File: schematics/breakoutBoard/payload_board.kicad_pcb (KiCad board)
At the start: 2 copper layers, 75 x 107 mm, 19 parts, among them P1 CONN_02X50, P2 CONN_02X50, P3 CONN_02X50, P4 CONN_02X50, U1 breakout_carrier

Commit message: 'final' push
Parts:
- removed RIB1: B5B-EH-A, breakoutBoard:B5B-EH-A
- added SMA2: Molex-MMCX-SMD, breakoutBoard:Molex MMCX SMD 50Ohm, F.Cu at (113.0, 154.0)
- added e1: ribbon2.54mmPitch, breakoutBoard:ribbon2.5mmPitch, F.Cu at (87.4, 154.2)
- moved SMA1 6.17 mm to (103.0, 154.0)
- moved U1 4.46 mm to (61.0, 153.2)
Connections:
- P1 pad 79: Net-(P1-Pad79) -> Net-(P1-Pad78)
- P1 pad 80: Net-(P1-Pad80) -> Net-(P1-Pad78)
- P1 pad 95: Net-(P1-Pad95) -> Net-(P1-Pad78)
- P2 pad 78: Net-(P2-Pad78) -> Net-(P1-Pad78)
- P2 pad 79: Net-(P2-Pad79) -> Net-(P1-Pad78)
- P2 pad 80: Net-(P2-Pad80) -> Net-(P1-Pad78)
- P2 pad 98: Net-(P2-Pad98) -> Net-(P1-Pad78)
- P3 pad 11: Net-(P3-Pad11) -> Net-(P1-Pad78)
- P3 pad 30: Net-(P3-Pad30) -> Net-(P1-Pad78)
- P3 pad 32: Net-(P3-Pad32) -> Net-(P1-Pad78)
- P3 pad 45: Net-(P3-Pad45) -> Net-(P1-Pad78)
- P3 pad 46: Net-(P3-Pad46) -> Net-(P1-Pad78)
- P3 pad 5: Net-(P3-Pad5) -> Net-(P1-Pad78)
- P3 pad 7: Net-(P3-Pad7) -> Net-(P1-Pad78)
- P3 pad 9: Net-(P3-Pad9) -> Net-(P1-Pad78)
- SMA1 pad 1: Net-(P1-Pad92) -> Net-(SMA1-Pad1)
- SMA1 pad 2: Net-(P1-Pad94) -> Net-(SMA1-Pad2)
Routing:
- net Net-(P1-Pad78): track 0.00 -> 257.8 mm, vias 0 -> 1
- net Net-(P4-Pad99): track 0.00 -> 68.2 mm
- net Net-(P1-Pad95): track 63.9 -> 0.00 mm, vias 1 -> 0
- net Net-(P4-Pad98): track 0.00 -> 51.8 mm
- net Net-(P2-Pad17): track 100.6 -> 115.0 mm
- net Net-(SMA1-Pad1): track 0.00 -> 10.0 mm
- net Net-(P1-Pad5): track 110.9 -> 115.7 mm
- net Net-(P1-Pad57): track 146.3 -> 143.3 mm, vias 2 -> 3
- net Net-(P2-Pad19): track 103.3 -> 100.8 mm, vias 0 -> 1
- added copper zone on B.Cu, net Net-(SMA1-Pad2)
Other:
- board text added: "5V"
- board text added: "CySat 488 Team: Trent Allison Brian Bradford"
- board text added: "Jared Danner Leo Freier"
- board text added: "UARTRX"
- board text added: "UARTTX"

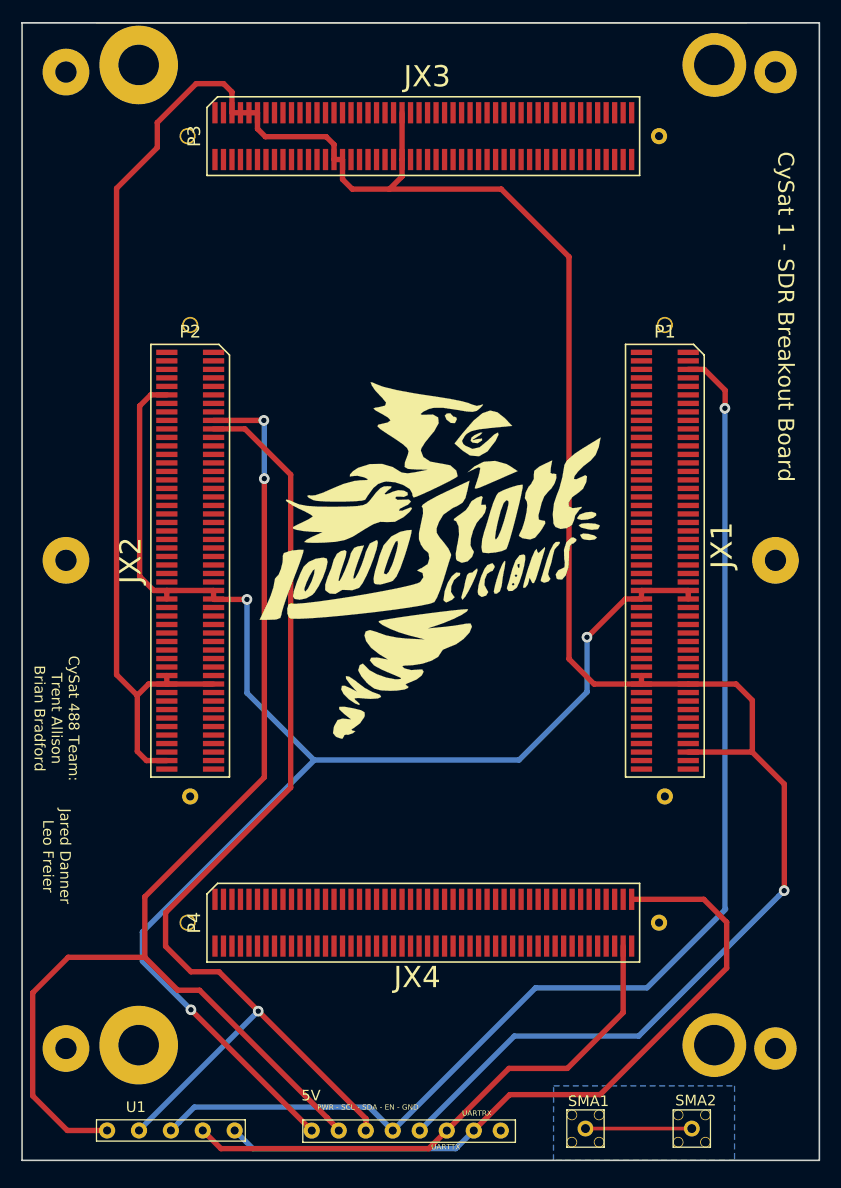
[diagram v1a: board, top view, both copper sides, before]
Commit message: final board v2, now with UART
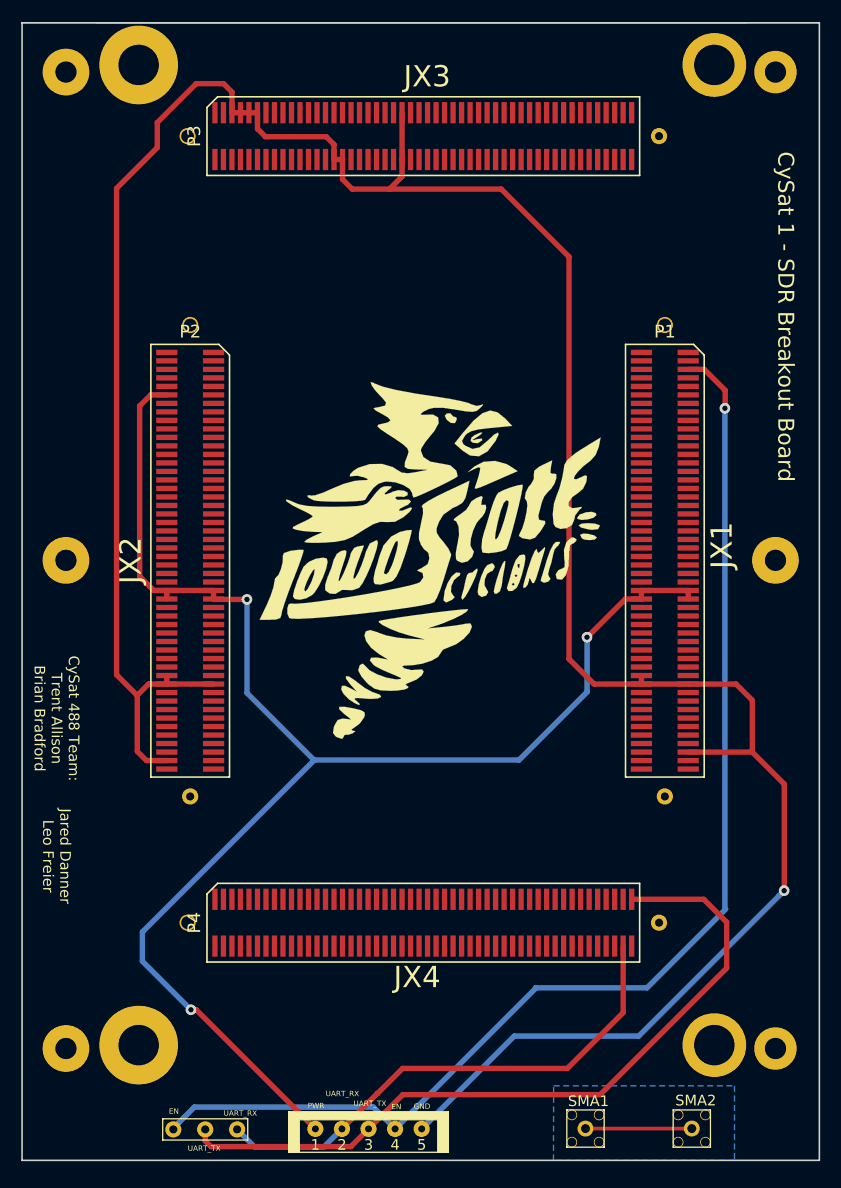
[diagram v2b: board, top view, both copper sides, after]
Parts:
- removed e1: ribbon2.54mmPitch, breakoutBoard:ribbon2.5mmPitch
- added RIB1: B5B-EH-A, breakoutBoard:B5B-EH-A, F.Cu at (75.1, 152.4)
- moved U1 6.23 mm to (67.2, 153.1)
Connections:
- U1 pad 1: Net-(P2-Pad17) -> Net-(P1-Pad5)
- U1 pad 2: Net-(P2-Pad19) -> Net-(P4-Pad99)
- U1 pad 3: Net-(P1-Pad5) -> Net-(P4-Pad98)
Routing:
- net Net-(P2-Pad17): track 115.0 -> 0.00 mm, vias 2 -> 0
- net Net-(P2-Pad19): track 100.8 -> 0.00 mm, vias 1 -> 0
- net Net-(P4-Pad98): track 51.8 -> 48.5 mm
- net Net-(P4-Pad99): track 68.2 -> 71.5 mm
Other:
- board text added: "EN"
- board text added: "GND"
- board text added: "PWR"
- board text added: "UART_RX"
- board text added: "UART_TX"
- board text removed: "5V"
- board text removed: "PWR - SCL - SDA - EN - GND"
- board text removed: "UARTRX"
- board text removed: "UARTTX"

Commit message: Files updated based on recent version sent to fab house
This more recent revision fixes the FPGA connector issue and adds the LNA board to the backside. Board was changed from a 2-layer to a 4-layer board due to the additional RF components added.
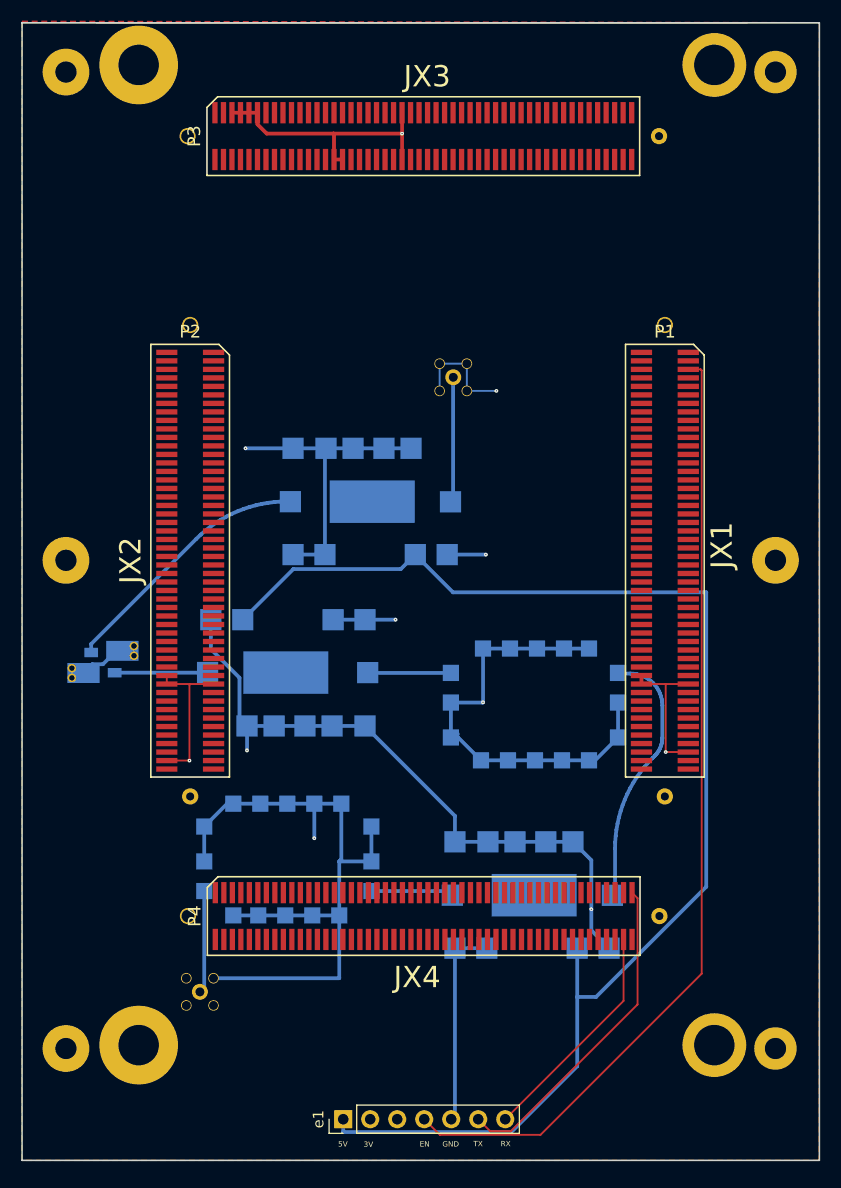
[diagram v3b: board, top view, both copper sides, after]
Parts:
- removed G*** (x2): LOGO, breakoutBoard:Cysized
- removed RIB1: B5B-EH-A, breakoutBoard:B5B-EH-A
- added U2: TAMP, mini-circuits:MCL, B.Cu at (98.0, 132.1)
- added U3: CBP, mini-circuits:CBP, B.Cu at (98.4, 113.9)
- added U4: TAMP, mini-circuits:MCL, B.Cu at (74.9, 111.1)
- added U5: LAT-3, RF_Mini-Circuits:Mini-Circuits_MMM168_LandPatternPL-225, B.Cu at (57.6, 110.2)
- added U6: TAMP, mini-circuits:MCL, B.Cu at (82.8, 95.1)
- added e1: ribbon2.54mmPitch, Connector_PinHeader_2.54mm:PinHeader_1x07_P2.54mm_Vertical, F.Cu at (80.2, 153.1)
- SMA1, SMA2: moved to B.Cu
- U1: value breakout_carrier -> CBP; footprint breakoutBoard:breakout_carrier -> mini-circuits:CBP; moved to B.Cu
- moved SMA2 74.1 mm to (90.6, 83.3)
- moved SMA1 38.5 mm to (66.7, 141.2)
- moved U1 25.4 mm to (74.8, 128.9)
- moved P4 0.63 mm to (87.8, 134.0)
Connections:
- net Net-(P1-Pad57) renamed 3V
- net Net-(P1-Pad78) renamed GND
- P1 pad 1: Net-(P1-Pad1) -> (no net)
- P1 pad 10: Net-(P1-Pad10) -> (no net)
- P1 pad 100: Net-(P1-Pad100) -> (no net)
- P1 pad 11: Net-(P1-Pad11) -> (no net)
- P1 pad 12: Net-(P1-Pad12) -> (no net)
- P1 pad 13: Net-(P1-Pad13) -> (no net)
- P1 pad 14: Net-(P1-Pad14) -> (no net)
- P1 pad 15: Net-(P1-Pad15) -> (no net)
- P1 pad 16: Net-(P1-Pad16) -> (no net)
- P1 pad 17: Net-(P1-Pad17) -> (no net)
- P1 pad 18: Net-(P1-Pad18) -> (no net)
- P1 pad 19: Net-(P1-Pad19) -> (no net)
- P1 pad 2: Net-(P1-Pad2) -> (no net)
- P1 pad 20: Net-(P1-Pad20) -> (no net)
- P1 pad 21: Net-(P1-Pad21) -> (no net)
- P1 pad 22: Net-(P1-Pad22) -> (no net)
- P1 pad 23: Net-(P1-Pad23) -> (no net)
- P1 pad 24: Net-(P1-Pad24) -> (no net)
- P1 pad 25: Net-(P1-Pad25) -> (no net)
- P1 pad 26: Net-(P1-Pad26) -> (no net)
- P1 pad 27: Net-(P1-Pad27) -> (no net)
- P1 pad 28: Net-(P1-Pad28) -> (no net)
- P1 pad 29: Net-(P1-Pad29) -> (no net)
- P1 pad 3: Net-(P1-Pad3) -> (no net)
- P1 pad 30: Net-(P1-Pad30) -> (no net)
- P1 pad 31: Net-(P1-Pad31) -> (no net)
- P1 pad 32: Net-(P1-Pad32) -> (no net)
- P1 pad 33: Net-(P1-Pad33) -> (no net)
- P1 pad 34: Net-(P1-Pad34) -> (no net)
- P1 pad 35: Net-(P1-Pad35) -> (no net)
- P1 pad 36: Net-(P1-Pad36) -> (no net)
- P1 pad 37: Net-(P1-Pad37) -> (no net)
- P1 pad 38: Net-(P1-Pad38) -> (no net)
- P1 pad 39: Net-(P1-Pad39) -> (no net)
- P1 pad 4: Net-(P1-Pad4) -> (no net)
- P1 pad 40: Net-(P1-Pad40) -> (no net)
- P1 pad 41: Net-(P1-Pad41) -> (no net)
- P1 pad 42: Net-(P1-Pad42) -> (no net)
- P1 pad 43: Net-(P1-Pad43) -> (no net)
- P1 pad 44: Net-(P1-Pad44) -> (no net)
- P1 pad 45: Net-(P1-Pad45) -> (no net)
- P1 pad 46: Net-(P1-Pad46) -> (no net)
- P1 pad 47: Net-(P1-Pad47) -> (no net)
- P1 pad 48: Net-(P1-Pad48) -> (no net)
- P1 pad 49: Net-(P1-Pad49) -> (no net)
- P1 pad 5: Net-(P1-Pad5) -> EN
- P1 pad 50: Net-(P1-Pad50) -> (no net)
- P1 pad 51: Net-(P1-Pad51) -> (no net)
- P1 pad 52: Net-(P1-Pad52) -> (no net)
- P1 pad 53: Net-(P1-Pad53) -> (no net)
- P1 pad 54: Net-(P1-Pad54) -> (no net)
- P1 pad 55: Net-(P1-Pad55) -> (no net)
- P1 pad 56: Net-(P1-Pad56) -> (no net)
- P1 pad 6: Net-(P1-Pad6) -> (no net)
- P1 pad 61: Net-(P1-Pad61) -> (no net)
- P1 pad 62: Net-(P1-Pad62) -> (no net)
- P1 pad 63: Net-(P1-Pad63) -> (no net)
- P1 pad 64: Net-(P1-Pad64) -> (no net)
- P1 pad 65: Net-(P1-Pad65) -> (no net)
- P1 pad 66: Net-(P1-Pad66) -> (no net)
- P1 pad 67: Net-(P1-Pad67) -> (no net)
- P1 pad 68: Net-(P1-Pad68) -> (no net)
- P1 pad 69: Net-(P1-Pad69) -> (no net)
- P1 pad 7: Net-(P1-Pad7) -> (no net)
- P1 pad 70: Net-(P1-Pad70) -> (no net)
- P1 pad 71: Net-(P1-Pad71) -> (no net)
- P1 pad 72: Net-(P1-Pad72) -> (no net)
- P1 pad 73: Net-(P1-Pad73) -> (no net)
- P1 pad 74: Net-(P1-Pad74) -> (no net)
- P1 pad 75: Net-(P1-Pad75) -> (no net)
- P1 pad 76: Net-(P1-Pad76) -> (no net)
- P1 pad 77: Net-(P1-Pad77) -> (no net)
- P1 pad 8: Net-(P1-Pad8) -> (no net)
- P1 pad 81: Net-(P1-Pad81) -> (no net)
- P1 pad 82: Net-(P1-Pad82) -> (no net)
- P1 pad 83: Net-(P1-Pad83) -> (no net)
- P1 pad 84: Net-(P1-Pad84) -> (no net)
- P1 pad 85: Net-(P1-Pad85) -> (no net)
- P1 pad 86: Net-(P1-Pad86) -> (no net)
- P1 pad 87: Net-(P1-Pad87) -> (no net)
- P1 pad 88: Net-(P1-Pad88) -> (no net)
- P1 pad 89: Net-(P1-Pad89) -> (no net)
- P1 pad 9: Net-(P1-Pad9) -> (no net)
- P1 pad 90: Net-(P1-Pad90) -> (no net)
- P1 pad 91: Net-(P1-Pad91) -> (no net)
- P1 pad 92: Net-(P1-Pad92) -> (no net)
- P1 pad 93: Net-(P1-Pad93) -> (no net)
- P1 pad 94: Net-(P1-Pad94) -> (no net)
- P1 pad 96: Net-(P1-Pad96) -> (no net)
- P1 pad 97: Net-(P1-Pad97) -> (no net)
- P1 pad 98: Net-(P1-Pad98) -> (no net)
- P1 pad 99: Net-(P1-Pad99) -> (no net)
- P2 pad 1: Net-(P2-Pad1) -> (no net)
- P2 pad 10: Net-(P2-Pad10) -> (no net)
- P2 pad 100: Net-(P2-Pad100) -> (no net)
- P2 pad 11: Net-(P2-Pad11) -> (no net)
- P2 pad 13: Net-(P2-Pad13) -> (no net)
- P2 pad 14: Net-(P2-Pad14) -> (no net)
- P2 pad 15: Net-(P2-Pad15) -> (no net)
- P2 pad 16: Net-(P2-Pad16) -> (no net)
- P2 pad 17: Net-(P2-Pad17) -> (no net)
- P2 pad 18: Net-(P2-Pad18) -> (no net)
- P2 pad 19: Net-(P2-Pad19) -> (no net)
- P2 pad 2: Net-(P2-Pad2) -> (no net)
- P2 pad 20: Net-(P2-Pad20) -> (no net)
- P2 pad 21: Net-(P2-Pad21) -> (no net)
- P2 pad 22: Net-(P2-Pad22) -> (no net)
- P2 pad 23: Net-(P2-Pad23) -> (no net)
- P2 pad 24: Net-(P2-Pad24) -> (no net)
- P2 pad 25: Net-(P2-Pad25) -> (no net)
- P2 pad 26: Net-(P2-Pad26) -> (no net)
- P2 pad 27: Net-(P2-Pad27) -> (no net)
- P2 pad 28: Net-(P2-Pad28) -> (no net)
- P2 pad 29: Net-(P2-Pad29) -> (no net)
- P2 pad 3: Net-(P2-Pad3) -> (no net)
- P2 pad 30: Net-(P2-Pad30) -> (no net)
- P2 pad 31: Net-(P2-Pad31) -> (no net)
- P2 pad 32: Net-(P2-Pad32) -> (no net)
- P2 pad 33: Net-(P2-Pad33) -> (no net)
- P2 pad 34: Net-(P2-Pad34) -> (no net)
- P2 pad 35: Net-(P2-Pad35) -> (no net)
- P2 pad 36: Net-(P2-Pad36) -> (no net)
- P2 pad 37: Net-(P2-Pad37) -> (no net)
- P2 pad 38: Net-(P2-Pad38) -> (no net)
- P2 pad 39: Net-(P2-Pad39) -> (no net)
- P2 pad 4: Net-(P2-Pad4) -> (no net)
- P2 pad 40: Net-(P2-Pad40) -> (no net)
- P2 pad 41: Net-(P2-Pad41) -> (no net)
- P2 pad 42: Net-(P2-Pad42) -> (no net)
- P2 pad 43: Net-(P2-Pad43) -> (no net)
- P2 pad 44: Net-(P2-Pad44) -> (no net)
- P2 pad 45: Net-(P2-Pad45) -> (no net)
- P2 pad 46: Net-(P2-Pad46) -> (no net)
- P2 pad 47: Net-(P2-Pad47) -> (no net)
- P2 pad 48: Net-(P2-Pad48) -> (no net)
- P2 pad 49: Net-(P2-Pad49) -> (no net)
- P2 pad 5: Net-(P2-Pad5) -> (no net)
- P2 pad 50: Net-(P2-Pad50) -> (no net)
- P2 pad 51: Net-(P2-Pad51) -> (no net)
- P2 pad 52: Net-(P2-Pad52) -> (no net)
- P2 pad 53: Net-(P2-Pad53) -> (no net)
- P2 pad 54: Net-(P2-Pad54) -> (no net)
- P2 pad 55: Net-(P2-Pad55) -> (no net)
- P2 pad 56: Net-(P2-Pad56) -> (no net)
- P2 pad 6: Net-(P2-Pad6) -> (no net)
- P2 pad 61: Net-(P2-Pad61) -> (no net)
- P2 pad 62: Net-(P2-Pad62) -> (no net)
- P2 pad 63: Net-(P2-Pad63) -> (no net)
- P2 pad 64: Net-(P2-Pad64) -> (no net)
- P2 pad 65: Net-(P2-Pad65) -> (no net)
- P2 pad 66: Net-(P2-Pad66) -> (no net)
- P2 pad 67: Net-(P2-Pad67) -> (no net)
- P2 pad 68: Net-(P2-Pad68) -> (no net)
- P2 pad 69: Net-(P2-Pad69) -> (no net)
- P2 pad 7: Net-(P2-Pad7) -> (no net)
- P2 pad 70: Net-(P2-Pad70) -> (no net)
- P2 pad 71: Net-(P2-Pad71) -> (no net)
- P2 pad 72: Net-(P2-Pad72) -> (no net)
- P2 pad 73: Net-(P2-Pad73) -> (no net)
- P2 pad 74: Net-(P2-Pad74) -> (no net)
- P2 pad 75: Net-(P2-Pad75) -> (no net)
- P2 pad 76: Net-(P2-Pad76) -> (no net)
- P2 pad 77: Net-(P2-Pad77) -> (no net)
- P2 pad 8: Net-(P2-Pad8) -> (no net)
- P2 pad 81: Net-(P2-Pad81) -> (no net)
- P2 pad 82: Net-(P2-Pad82) -> (no net)
- P2 pad 83: Net-(P2-Pad83) -> (no net)
- P2 pad 84: Net-(P2-Pad84) -> (no net)
- P2 pad 85: Net-(P2-Pad85) -> (no net)
- P2 pad 86: Net-(P2-Pad86) -> (no net)
- P2 pad 87: Net-(P2-Pad87) -> (no net)
- P2 pad 88: Net-(P2-Pad88) -> (no net)
- P2 pad 89: Net-(P2-Pad89) -> (no net)
- P2 pad 9: Net-(P2-Pad9) -> (no net)
- P2 pad 90: Net-(P2-Pad90) -> (no net)
- P2 pad 91: Net-(P2-Pad91) -> (no net)
- P2 pad 92: Net-(P2-Pad92) -> (no net)
- P2 pad 93: Net-(P2-Pad93) -> (no net)
- P2 pad 94: Net-(P2-Pad94) -> (no net)
- P2 pad 95: Net-(P2-Pad95) -> (no net)
- P2 pad 96: Net-(P2-Pad96) -> (no net)
- P2 pad 97: Net-(P2-Pad97) -> (no net)
- P2 pad 99: Net-(P2-Pad99) -> (no net)
- P3 pad 1: Net-(P3-Pad1) -> (no net)
- P3 pad 10: Net-(P3-Pad10) -> (no net)
- P3 pad 100: Net-(P3-Pad100) -> (no net)
- P3 pad 12: Net-(P3-Pad12) -> (no net)
- P3 pad 13: Net-(P3-Pad13) -> (no net)
- P3 pad 14: Net-(P3-Pad14) -> (no net)
- P3 pad 15: Net-(P3-Pad15) -> (no net)
- P3 pad 16: Net-(P3-Pad16) -> (no net)
- P3 pad 17: Net-(P3-Pad17) -> (no net)
- P3 pad 18: Net-(P3-Pad18) -> (no net)
- P3 pad 19: Net-(P3-Pad19) -> (no net)
- P3 pad 2: Net-(P3-Pad2) -> (no net)
- P3 pad 20: Net-(P3-Pad20) -> (no net)
- P3 pad 21: Net-(P3-Pad21) -> (no net)
- P3 pad 22: Net-(P3-Pad22) -> (no net)
- P3 pad 23: Net-(P3-Pad23) -> (no net)
- P3 pad 24: Net-(P3-Pad24) -> (no net)
- P3 pad 25: Net-(P3-Pad25) -> (no net)
- P3 pad 26: Net-(P3-Pad26) -> (no net)
- P3 pad 27: Net-(P3-Pad27) -> (no net)
- P3 pad 28: Net-(P3-Pad28) -> (no net)
- P3 pad 29: Net-(P3-Pad29) -> (no net)
- P3 pad 3: Net-(P3-Pad3) -> (no net)
- P3 pad 31: Net-(P3-Pad31) -> (no net)
- P3 pad 33: Net-(P3-Pad33) -> (no net)
- P3 pad 34: Net-(P3-Pad34) -> (no net)
- P3 pad 35: Net-(P3-Pad35) -> (no net)
- P3 pad 36: Net-(P3-Pad36) -> (no net)
- P3 pad 37: Net-(P3-Pad37) -> (no net)
- P3 pad 38: Net-(P3-Pad38) -> (no net)
- P3 pad 39: Net-(P3-Pad39) -> (no net)
- P3 pad 4: Net-(P3-Pad4) -> (no net)
- P3 pad 40: Net-(P3-Pad40) -> (no net)
- P3 pad 41: Net-(P3-Pad41) -> (no net)
- P3 pad 42: Net-(P3-Pad42) -> (no net)
- P3 pad 43: Net-(P3-Pad43) -> (no net)
- P3 pad 44: Net-(P3-Pad44) -> (no net)
- P3 pad 47: Net-(P3-Pad47) -> (no net)
- P3 pad 48: Net-(P3-Pad48) -> (no net)
- P3 pad 49: Net-(P3-Pad49) -> (no net)
- P3 pad 50: Net-(P3-Pad50) -> (no net)
- P3 pad 51: Net-(P3-Pad51) -> (no net)
- P3 pad 52: Net-(P3-Pad52) -> (no net)
- P3 pad 53: Net-(P3-Pad53) -> (no net)
- P3 pad 54: Net-(P3-Pad54) -> (no net)
- P3 pad 55: Net-(P3-Pad55) -> (no net)
- P3 pad 56: Net-(P3-Pad56) -> (no net)
- P3 pad 57: Net-(P3-Pad57) -> (no net)
- P3 pad 58: Net-(P3-Pad58) -> (no net)
- P3 pad 59: Net-(P3-Pad59) -> (no net)
- P3 pad 6: Net-(P3-Pad6) -> (no net)
- P3 pad 60: Net-(P3-Pad60) -> (no net)
- P3 pad 61: Net-(P3-Pad61) -> (no net)
- P3 pad 62: Net-(P3-Pad62) -> (no net)
- P3 pad 63: Net-(P3-Pad63) -> (no net)
- P3 pad 64: Net-(P3-Pad64) -> (no net)
- P3 pad 65: Net-(P3-Pad65) -> (no net)
- P3 pad 66: Net-(P3-Pad66) -> (no net)
- P3 pad 67: Net-(P3-Pad67) -> (no net)
- P3 pad 68: Net-(P3-Pad68) -> (no net)
- P3 pad 69: Net-(P3-Pad69) -> (no net)
- P3 pad 70: Net-(P3-Pad70) -> (no net)
- P3 pad 71: Net-(P3-Pad71) -> (no net)
- P3 pad 72: Net-(P3-Pad72) -> (no net)
- P3 pad 73: Net-(P3-Pad73) -> (no net)
- P3 pad 74: Net-(P3-Pad74) -> (no net)
- P3 pad 75: Net-(P3-Pad75) -> (no net)
- P3 pad 76: Net-(P3-Pad76) -> (no net)
- P3 pad 77: Net-(P3-Pad77) -> (no net)
- P3 pad 78: Net-(P3-Pad78) -> (no net)
- P3 pad 79: Net-(P3-Pad79) -> (no net)
- P3 pad 8: Net-(P3-Pad8) -> (no net)
- P3 pad 80: Net-(P3-Pad80) -> (no net)
- P3 pad 81: Net-(P3-Pad81) -> (no net)
- P3 pad 82: Net-(P3-Pad82) -> (no net)
- P3 pad 83: Net-(P3-Pad83) -> (no net)
- P3 pad 84: Net-(P3-Pad84) -> (no net)
- P3 pad 85: Net-(P3-Pad85) -> (no net)
- P3 pad 86: Net-(P3-Pad86) -> (no net)
- P3 pad 87: Net-(P3-Pad87) -> (no net)
- P3 pad 88: Net-(P3-Pad88) -> (no net)
- P3 pad 89: Net-(P3-Pad89) -> (no net)
- P3 pad 90: Net-(P3-Pad90) -> (no net)
- P3 pad 91: Net-(P3-Pad91) -> (no net)
- P3 pad 92: Net-(P3-Pad92) -> (no net)
- P3 pad 93: Net-(P3-Pad93) -> (no net)
- P3 pad 94: Net-(P3-Pad94) -> (no net)
- P3 pad 95: Net-(P3-Pad95) -> (no net)
- P3 pad 96: Net-(P3-Pad96) -> (no net)
- P3 pad 97: Net-(P3-Pad97) -> (no net)
- P3 pad 98: Net-(P3-Pad98) -> (no net)
- P3 pad 99: Net-(P3-Pad99) -> (no net)
- P4 pad 1: Net-(P4-Pad1) -> (no net)
- P4 pad 10: Net-(P4-Pad10) -> (no net)
- P4 pad 100: Net-(P4-Pad100) -> (no net)
- P4 pad 11: Net-(P4-Pad11) -> (no net)
- P4 pad 12: Net-(P4-Pad12) -> (no net)
- P4 pad 13: Net-(P4-Pad13) -> (no net)
- P4 pad 14: Net-(P4-Pad14) -> (no net)
- P4 pad 15: Net-(P4-Pad15) -> (no net)
- P4 pad 16: Net-(P4-Pad16) -> (no net)
- P4 pad 17: Net-(P4-Pad17) -> (no net)
- P4 pad 18: Net-(P4-Pad18) -> (no net)
- P4 pad 19: Net-(P4-Pad19) -> (no net)
- P4 pad 2: Net-(P4-Pad2) -> (no net)
- P4 pad 20: Net-(P4-Pad20) -> (no net)
- P4 pad 21: Net-(P4-Pad21) -> (no net)
- P4 pad 22: Net-(P4-Pad22) -> (no net)
- P4 pad 23: Net-(P4-Pad23) -> (no net)
- P4 pad 24: Net-(P4-Pad24) -> (no net)
- P4 pad 25: Net-(P4-Pad25) -> (no net)
- P4 pad 26: Net-(P4-Pad26) -> (no net)
- P4 pad 27: Net-(P4-Pad27) -> (no net)
- P4 pad 28: Net-(P4-Pad28) -> (no net)
- P4 pad 29: Net-(P4-Pad29) -> (no net)
- P4 pad 3: Net-(P4-Pad3) -> (no net)
- P4 pad 30: Net-(P4-Pad30) -> (no net)
- P4 pad 31: Net-(P4-Pad31) -> (no net)
- P4 pad 32: Net-(P4-Pad32) -> (no net)
- P4 pad 33: Net-(P4-Pad33) -> (no net)
- P4 pad 34: Net-(P4-Pad34) -> (no net)
- P4 pad 35: Net-(P4-Pad35) -> (no net)
- P4 pad 36: Net-(P4-Pad36) -> (no net)
- P4 pad 37: Net-(P4-Pad37) -> (no net)
- P4 pad 38: Net-(P4-Pad38) -> (no net)
- P4 pad 39: Net-(P4-Pad39) -> (no net)
- P4 pad 4: Net-(P4-Pad4) -> (no net)
- P4 pad 40: Net-(P4-Pad40) -> (no net)
- P4 pad 41: Net-(P4-Pad41) -> (no net)
- P4 pad 42: Net-(P4-Pad42) -> (no net)
- P4 pad 43: Net-(P4-Pad43) -> (no net)
- P4 pad 44: Net-(P4-Pad44) -> (no net)
- P4 pad 45: Net-(P4-Pad45) -> (no net)
- P4 pad 46: Net-(P4-Pad46) -> (no net)
- P4 pad 47: Net-(P4-Pad47) -> (no net)
- P4 pad 48: Net-(P4-Pad48) -> (no net)
- P4 pad 49: Net-(P4-Pad49) -> (no net)
- P4 pad 5: Net-(P4-Pad5) -> (no net)
- P4 pad 50: Net-(P4-Pad50) -> (no net)
- P4 pad 51: Net-(P4-Pad51) -> (no net)
- P4 pad 52: Net-(P4-Pad52) -> (no net)
- P4 pad 53: Net-(P4-Pad53) -> (no net)
- P4 pad 54: Net-(P4-Pad54) -> (no net)
- P4 pad 55: Net-(P4-Pad55) -> (no net)
- P4 pad 56: Net-(P4-Pad56) -> (no net)
- P4 pad 57: Net-(P4-Pad57) -> (no net)
- P4 pad 58: Net-(P4-Pad58) -> (no net)
- P4 pad 59: Net-(P4-Pad59) -> (no net)
- P4 pad 6: Net-(P4-Pad6) -> (no net)
- P4 pad 60: Net-(P4-Pad60) -> (no net)
- P4 pad 61: Net-(P4-Pad61) -> (no net)
- P4 pad 62: Net-(P4-Pad62) -> (no net)
- P4 pad 63: Net-(P4-Pad63) -> (no net)
- P4 pad 64: Net-(P4-Pad64) -> (no net)
- P4 pad 65: Net-(P4-Pad65) -> (no net)
- P4 pad 66: Net-(P4-Pad66) -> (no net)
- P4 pad 67: Net-(P4-Pad67) -> (no net)
- P4 pad 68: Net-(P4-Pad68) -> (no net)
- P4 pad 69: Net-(P4-Pad69) -> (no net)
- P4 pad 7: Net-(P4-Pad7) -> (no net)
- P4 pad 70: Net-(P4-Pad70) -> (no net)
- P4 pad 71: Net-(P4-Pad71) -> (no net)
- P4 pad 72: Net-(P4-Pad72) -> (no net)
- P4 pad 73: Net-(P4-Pad73) -> (no net)
- P4 pad 74: Net-(P4-Pad74) -> (no net)
- P4 pad 75: Net-(P4-Pad75) -> (no net)
- P4 pad 76: Net-(P4-Pad76) -> (no net)
- P4 pad 77: Net-(P4-Pad77) -> (no net)
- P4 pad 78: Net-(P4-Pad78) -> (no net)
- P4 pad 79: Net-(P4-Pad79) -> (no net)
- P4 pad 8: Net-(P4-Pad8) -> (no net)
- P4 pad 80: Net-(P4-Pad80) -> (no net)
- P4 pad 81: Net-(P4-Pad81) -> (no net)
- P4 pad 82: Net-(P4-Pad82) -> (no net)
- P4 pad 83: Net-(P4-Pad83) -> (no net)
- P4 pad 84: Net-(P4-Pad84) -> (no net)
- P4 pad 85: Net-(P4-Pad85) -> (no net)
- P4 pad 86: Net-(P4-Pad86) -> (no net)
- P4 pad 87: Net-(P4-Pad87) -> (no net)
- P4 pad 88: Net-(P4-Pad88) -> (no net)
- P4 pad 89: Net-(P4-Pad89) -> (no net)
- P4 pad 9: Net-(P4-Pad9) -> (no net)
- P4 pad 90: Net-(P4-Pad90) -> (no net)
- P4 pad 91: Net-(P4-Pad91) -> (no net)
- P4 pad 92: Net-(P4-Pad92) -> (no net)
- P4 pad 93: Net-(P4-Pad93) -> (no net)
- P4 pad 94: Net-(P4-Pad94) -> (no net)
- P4 pad 95: Net-(P4-Pad95) -> (no net)
- P4 pad 96: Net-(P4-Pad96) -> (no net)
- P4 pad 97: Net-(P4-Pad97) -> (no net)
- P4 pad 98: Net-(P4-Pad98) -> RX
- P4 pad 99: Net-(P4-Pad99) -> TX
- SMA1 pad 1: Net-(SMA1-Pad1) -> RF_SIG
- SMA1 pad 2: Net-(SMA1-Pad2) -> RFGND
- SMA2 pad 1: Net-(SMA1-Pad1) -> Net-(SMA2-Pad1)
- SMA2 pad 2: Net-(SMA1-Pad2) -> RFGND
- U1 pad 1: Net-(P1-Pad5) -> RF_SIG
- U1 pad 2: Net-(P4-Pad99) -> RFGND
- U1 pad 3: Net-(P4-Pad98) -> RFGND
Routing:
- net 3V: track 143.5 -> 0.00 mm, vias 3 -> 0
- net 5V: track 0.00 -> 128.6 mm
- net RFGND: track 0.00 -> 121.5 mm, vias 0 -> 3
- net Net-(P1-Pad5): track 115.7 -> 0.00 mm, vias 1 -> 0
- net EN: track 0.00 -> 91.1 mm
- net GND: track 257.6 -> 173.5 mm, vias 1 -> 8
- net Net-(P4-Pad99): track 71.5 -> 0.00 mm
- net Net-(P4-Pad98): track 48.5 -> 0.00 mm
- net TX: track 0.00 -> 31.1 mm
- net Net-(U5-Pad2): track 0.00 -> 25.8 mm
- net Net-(U2-Pad5): track 0.00 -> 25.7 mm
- net RX: track 0.00 -> 21.5 mm
- net Net-(SMA2-Pad1): track 0.00 -> 11.7 mm
- net RF_SIG: track 0.00 -> 10.3 mm
- net Net-(SMA1-Pad1): track 10.0 -> 0.00 mm
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- added copper zone on F.Cu, net 3V
- added copper zone on PGND, net GND
- added copper zone on RFGND, net RFGND
- removed copper zone on B.Cu, net Net-(SMA1-Pad2)
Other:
- copper layers 2 -> 4
- board text added: "3V"
- board text added: "5V"
- board text added: "RX"
- board text added: "TX"
- board text removed: "CySat 1 - SDR Breakout Board"
- board text removed: "CySat 488 Team: Trent Allison Brian Bradford"
- board text removed: "Jared Danner Leo Freier"
- board text removed: "PWR"
- board text removed: "UART_RX"
- board text removed: "UART_TX"

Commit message: Updated to FPGA connector
Rotated connectors to match what is on the board.
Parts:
- turned P1 to 90 degrees
- turned P2 to 90 degrees
- turned P4 to 180 degrees
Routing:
- net GND: track 173.5 -> 145.2 mm, vias 8 -> 5
- net TX: track 31.1 -> 3.54 mm
- net RX: track 21.5 -> 0.00 mm
- net (no net): track 0.00 -> 0.73 mm

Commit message: updates
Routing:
- net EN: track 91.1 -> 0.00 mm
- net GND: track 145.2 -> 161.5 mm
- net TX: track 3.54 -> 0.00 mm
- net (no net): track 0.73 -> 0.00 mm

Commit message: Final updates that were sent for fabrication
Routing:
- net RX: track 0.00 -> 64.2 mm
- net EN: track 0.00 -> 52.7 mm
- net GND: track 161.5 -> 195.8 mm, vias 5 -> 4
- net TX: track 0.00 -> 32.4 mm
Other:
- rule pad_to_mask_clearance: 0.2 -> 0

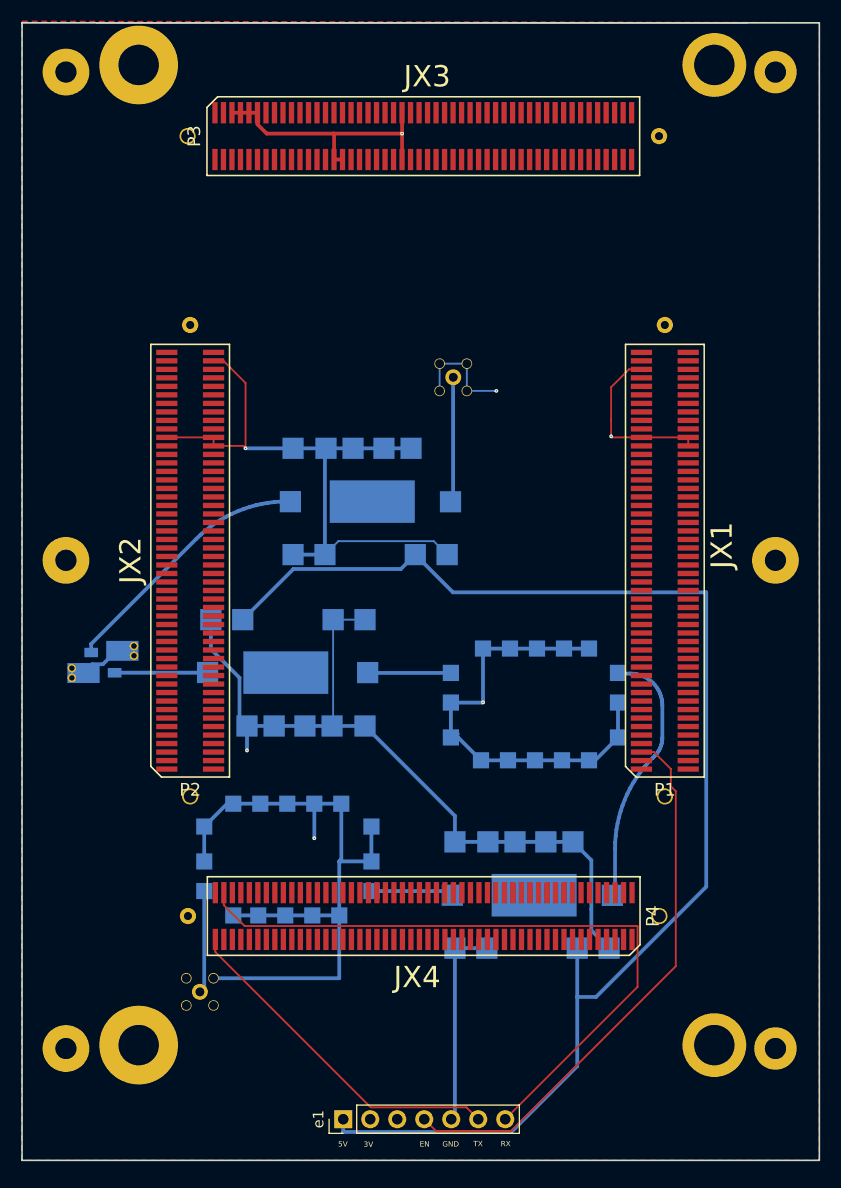
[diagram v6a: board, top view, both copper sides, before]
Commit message: Board fix
Board fix that was not uploaded to GitHub plus one slight modification to reduce the cutout from the TX/RX lines
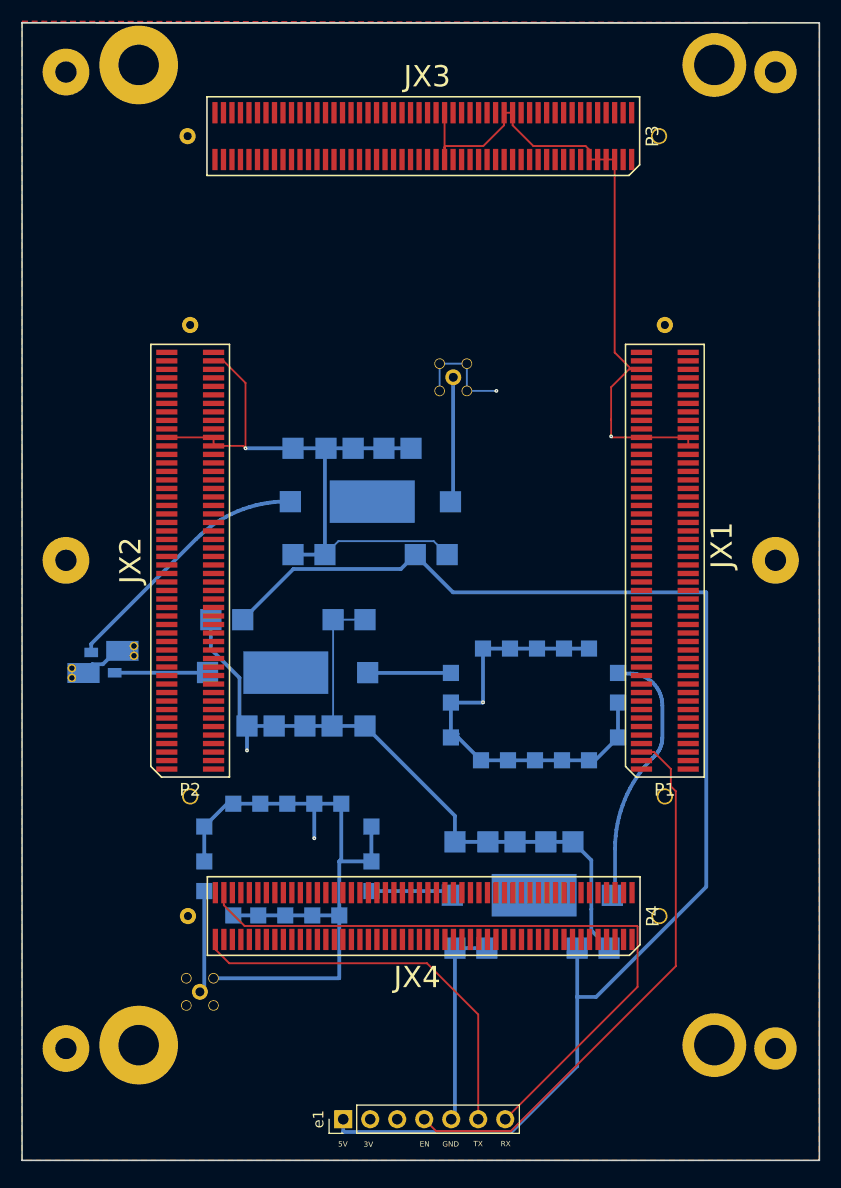
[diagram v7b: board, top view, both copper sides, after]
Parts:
- turned P3 to 180 degrees
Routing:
- net GND: track 195.8 -> 218.7 mm, vias 4 -> 3
- net TX: track 32.4 -> 38.0 mm

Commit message: Minor updates
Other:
- board text added: "FPGA and LNA Board Matthew E. Nelson Rev 5"
